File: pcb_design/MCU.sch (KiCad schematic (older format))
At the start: 17 parts, among them J9 SWD, SW1 BOOTLOADER, U1 STM32F40X_LQFP64, X2 ABM3B - 8MHz

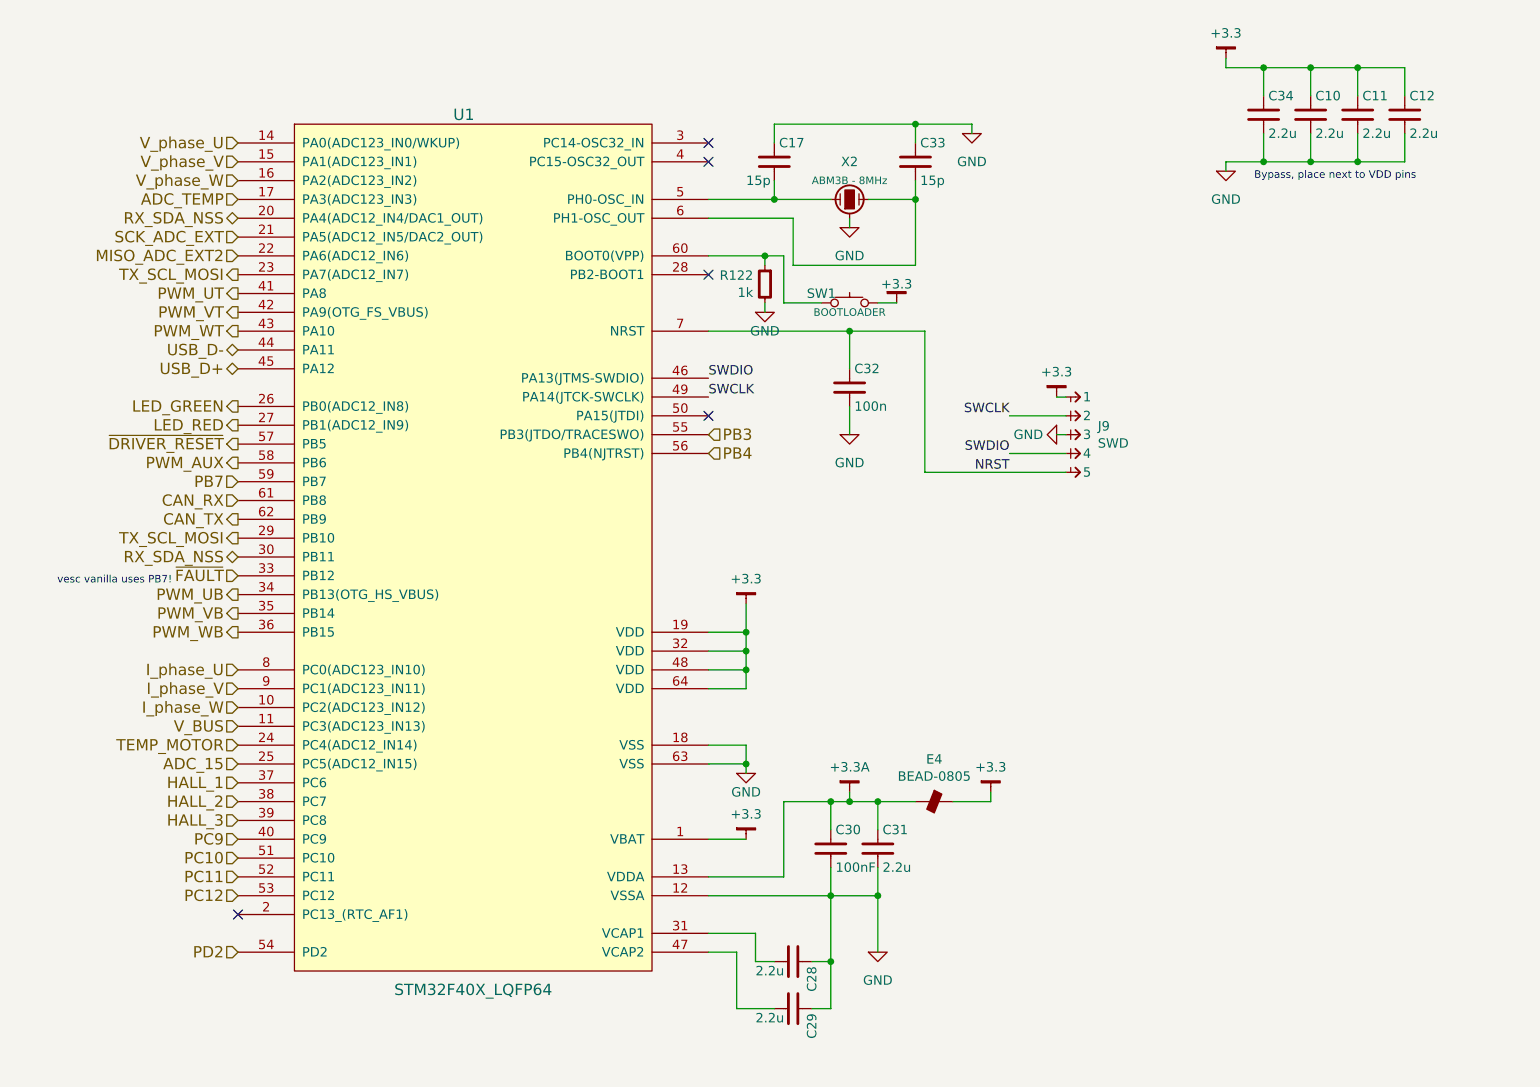
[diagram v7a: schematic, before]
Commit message: More layout. Changed LED pin. Added placeholder for a resolver IC
Signed-off-by: Marcos Chaparro <mchaparro@paltatech.com>
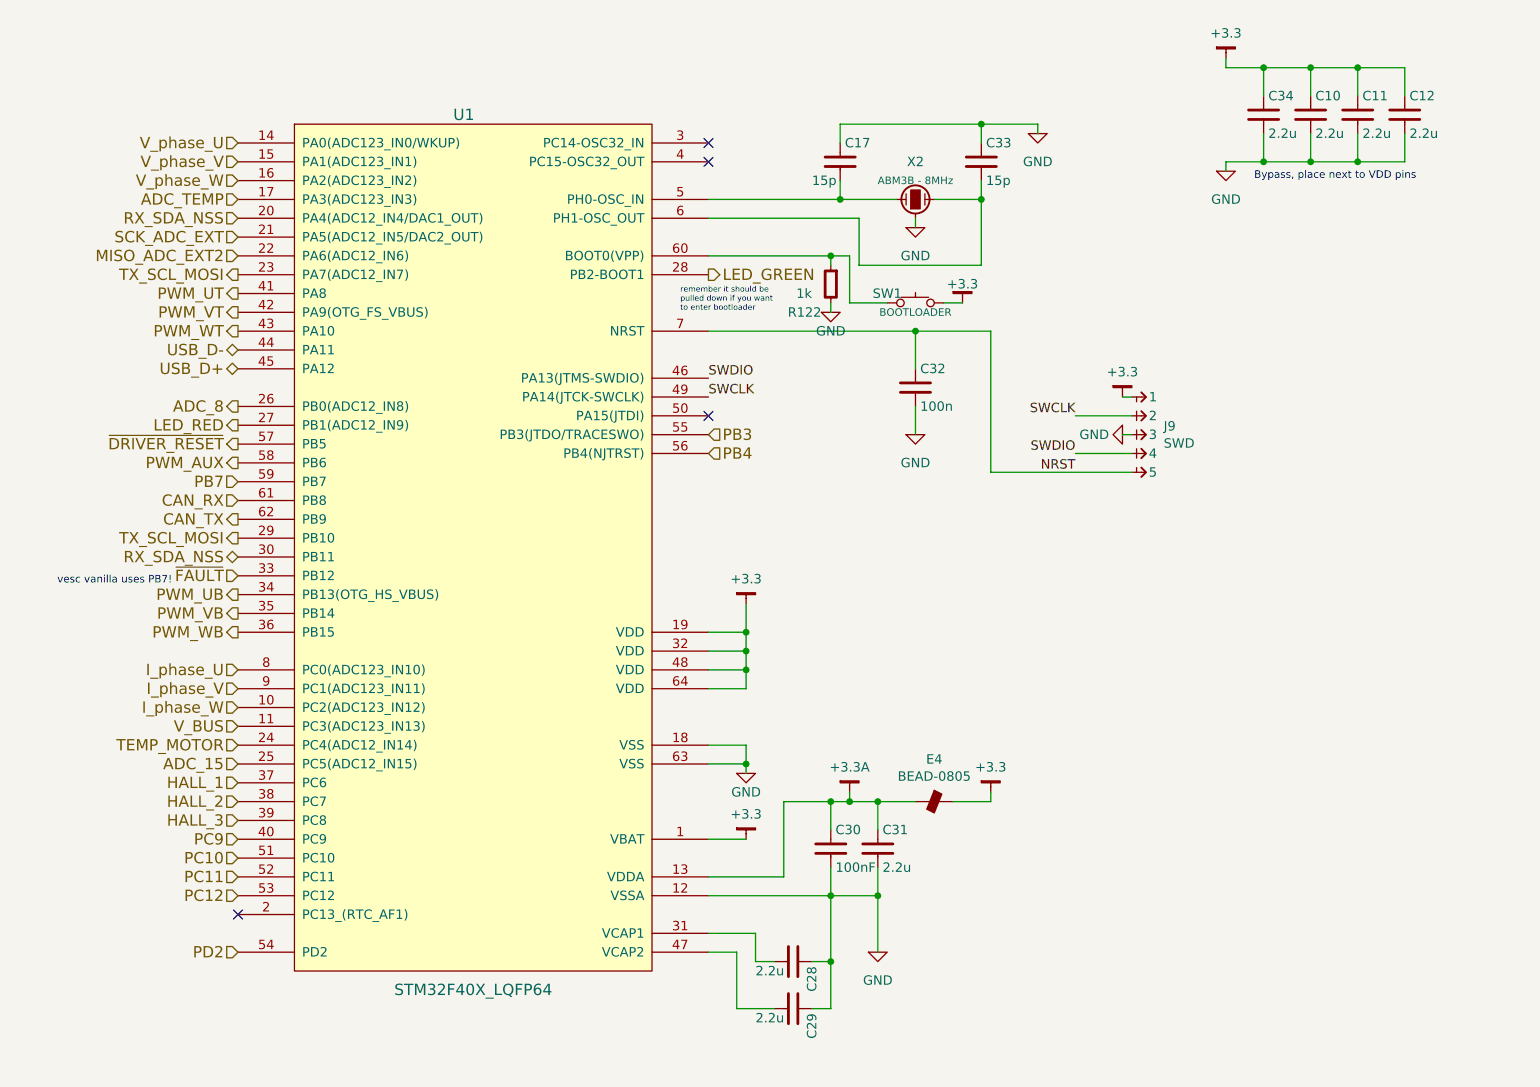
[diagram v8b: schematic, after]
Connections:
- net LED_GREEN: now also U1.28 (PB2-BOOT1); no longer U1.26 (PB0(ADC12_IN8))
- new net ADC_8: U1.26 (PB0(ADC12_IN8))
- no-connect marks 5 -> 4
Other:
- note added: "remember it should be\npulled down if you want\nto enter bootloader"
- moved on the sheet: C17, C32, C33, J9, R122, SW1, X2
